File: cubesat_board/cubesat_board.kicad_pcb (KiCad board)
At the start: 2 copper layers, 90 x 90 mm, 2 parts, among them J1 CONN_02X26, J2 CONN_02X26

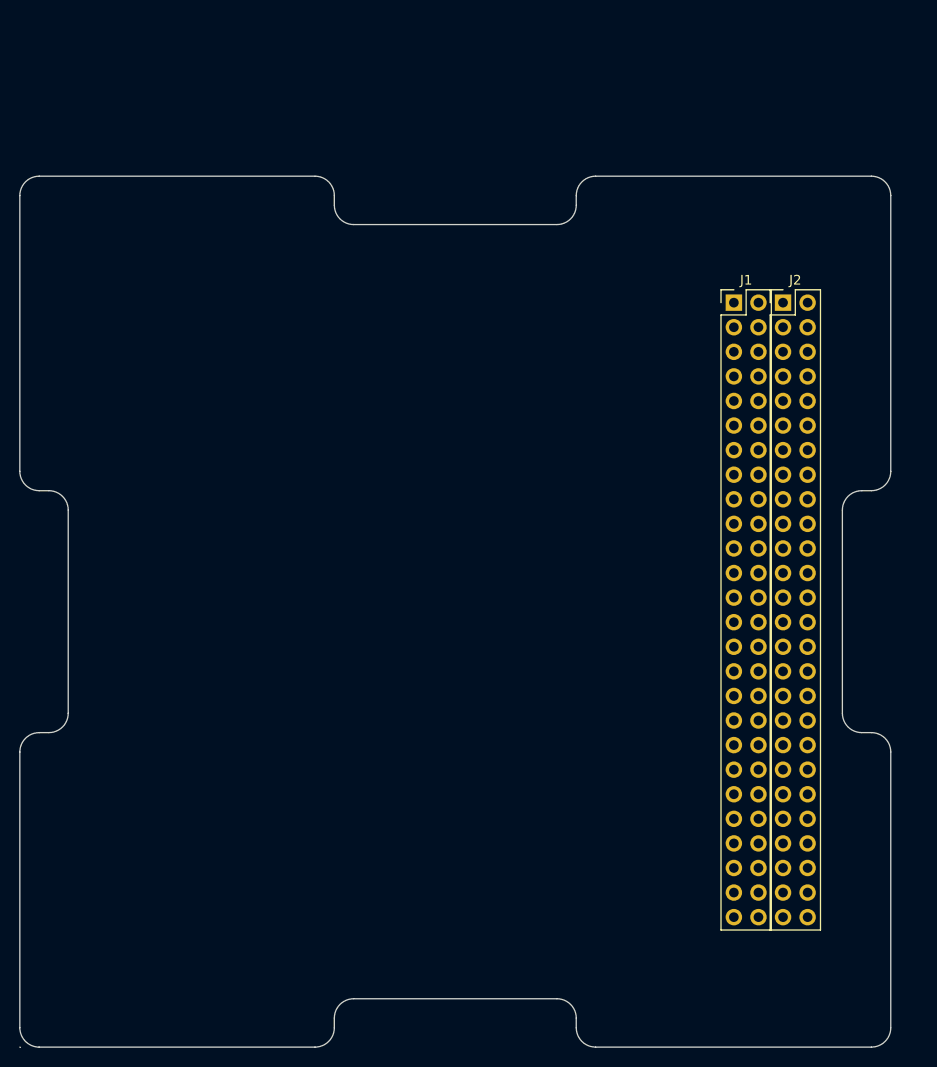
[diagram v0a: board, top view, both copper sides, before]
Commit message: New dxf without the slot behind the connector, updated board outline to new dxf and marked center of board as center of grids
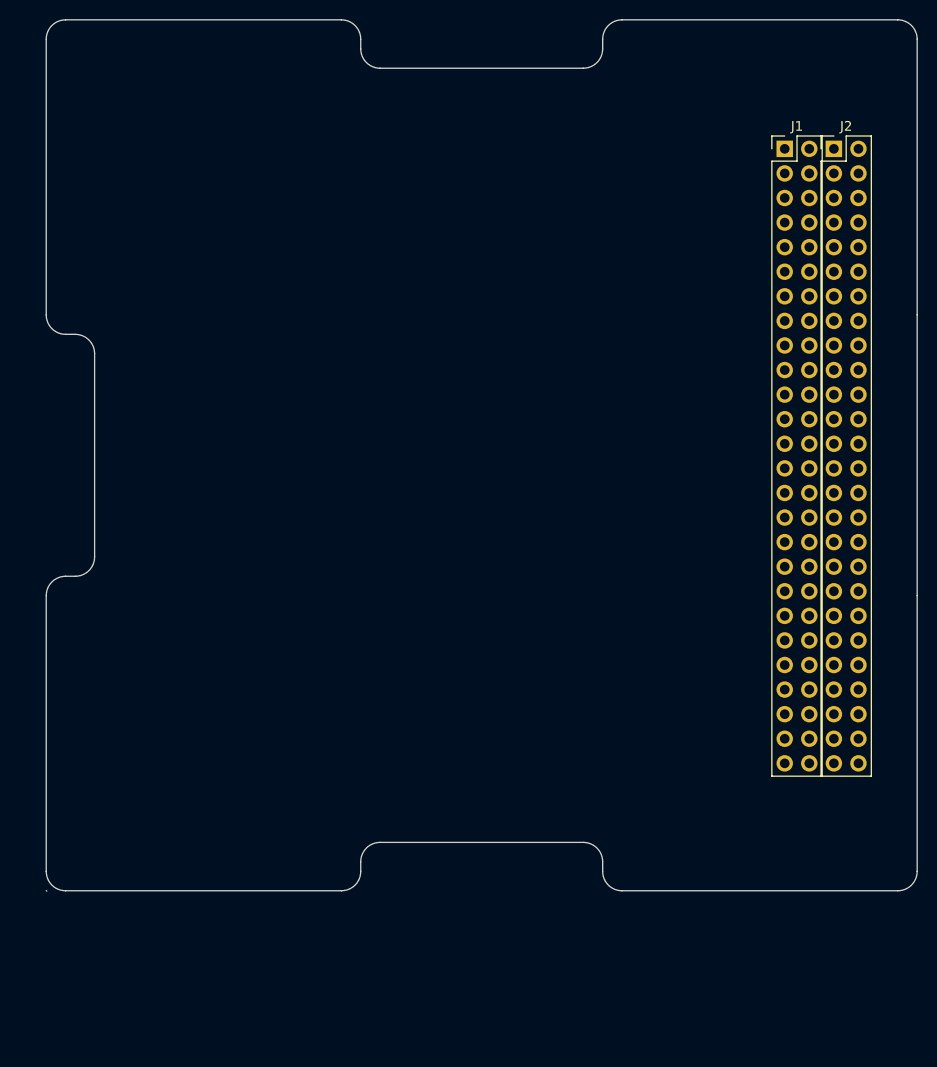
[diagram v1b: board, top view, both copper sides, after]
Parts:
- moved J2 16.7 mm to (172.9, 46.3)
- moved J1 16.7 mm to (167.8, 46.3)
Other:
- outline, holes or cut-outs redrawn
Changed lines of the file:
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@@
-(kicad_pcb (version 4) (host pcbnew 4.0.6)
+(kicad_pcb (version 4) (host pcbnew 4.0.7)
   (general
     (links 0)
     (no_connects 0)
-    (area 0 0 0 0)
+    (area 294.051667 73.53 309.198334 143.74)
     (thickness 1.6)
-    (drawings 41)
+    (drawings 35)
     (tracks 0)
     (zones 0)
@@
     (pad_drill 0.762)
     (pad_to_mask_clearance 0.2)
-    (aux_axis_origin 0 0)
-    (visible_elements FFFFFF7F)
+    (aux_axis_origin 136.5 78)
+    (grid_origin 136.5 78)
+    (visible_elements 7FFFFFFF)
     (pcbplotparams
       (layerselection 0x00030_80000001)
@@
   )
   (module Pin_Headers:Pin_Header_Straight_2x26_Pitch2.54mm (layer F.Cu)
-    (at 162.56 62.23)
+    (at 167.815 46.335)
     (descr "Through hole straight pin header, 2x26, 2.54mm pitch, double rows")
     (tags "Through hole pin header THT 2x26 2.54mm double row")
@@
   )
   (module Pin_Headers:Pin_Header_Straight_2x26_Pitch2.54mm (layer F.Cu)
-    (at 167.64 62.23)
+    (at 172.895 46.335)
     (descr "Through hole straight pin header, 2x26, 2.54mm pitch, double rows")
     (tags "Through hole pin header THT 2x26 2.54mm double row")
@@
     )
   )
-  (gr_line (start 91.773 106.660517) (end 90.773 106.660517) (layer Edge.Cuts) (width 0.1))
-  (gr_line (start 119.273 49.160517) (end 90.773 49.160517) (layer Edge.Cuts) (width 0.1))
-  (gr_line (start 178.773 79.660517) (end 178.773 51.160517) (layer Edge.Cuts) (width 0.1))
-  (gr_line (start 88.773 108.660517) (end 88.773 137.160517) (layer Edge.Cuts) (width 0.1))
-  (gr_line (start 88.773 51.160517) (end 88.773 79.660517) (layer Edge.Cuts) (width 0.1))
-  (gr_line (start 176.773 49.160517) (end 148.273 49.160517) (layer Edge.Cuts) (width 0.1))
-  (gr_line (start 146.273 52.160517) (end 146.273 51.160517) (layer Edge.Cuts) (width 0.1))
-  (gr_line (start 93.773 83.660517) (end 93.773 104.660517) (layer Edge.Cuts) (width 0.1))
-  (gr_line (start 121.273 52.160517) (end 121.273 51.160517) (layer Edge.Cuts) (width 0.1))
-  (gr_line (start 175.773 81.660517) (end 176.773 81.660517) (layer Edge.Cuts) (width 0.1))
-  (gr_line (start 88.773 139.160517) (end 88.832983 139.188433) (layer Edge.Cuts) (width 0.1))
-  (gr_line (start 90.773 81.660517) (end 91.773 81.660517) (layer Edge.Cuts) (width 0.1))
-  (gr_line (start 144.273 54.160517) (end 123.273 54.160517) (layer Edge.Cuts) (width 0.1))
-  (gr_arc (start 144.273 52.160517) (end 144.273 54.160517) (angle -90) (layer Edge.Cuts) (width 0.1))
-  (gr_line (start 148.273 139.160517) (end 176.773 139.160517) (layer Edge.Cuts) (width 0.1))
-  (gr_arc (start 175.773 104.660517) (end 173.773 104.660517) (angle -90) (layer Edge.Cuts) (width 0.1))
-  (gr_line (start 173.773 104.660517) (end 173.773 83.660517) (layer Edge.Cuts) (width 0.1))
-  (gr_arc (start 175.773 83.660517) (end 175.773 81.660517) (angle -90) (layer Edge.Cuts) (width 0.1))
-  (gr_arc (start 176.773 79.660517) (end 176.773 81.660517) (angle -90) (layer Edge.Cuts) (width 0.1))
-  (gr_line (start 146.273 136.160517) (end 146.273 137.160517) (layer Edge.Cuts) (width 0.1))
-  (gr_arc (start 90.773 108.660517) (end 90.773 106.660517) (angle -90) (layer Edge.Cuts) (width 0.1))
-  (gr_line (start 90.773 139.160517) (end 119.273 139.160517) (layer Edge.Cuts) (width 0.1))
-  (gr_line (start 176.773 106.660517) (end 175.773 106.660517) (layer Edge.Cuts) (width 0.1))
-  (gr_arc (start 176.773 51.160517) (end 178.773 51.160517) (angle -90) (layer Edge.Cuts) (width 0.1))
-  (gr_arc (start 148.273 137.160517) (end 146.273 137.160517) (angle -90) (layer Edge.Cuts) (width 0.1))
-  (gr_arc (start 90.773 79.660517) (end 88.773 79.660517) (angle -90) (layer Edge.Cuts) (width 0.1))
-  (gr_line (start 178.773 137.160517) (end 178.773 108.660517) (layer Edge.Cuts) (width 0.1))
-  (gr_arc (start 176.773 137.160517) (end 176.773 139.160517) (angle -90) (layer Edge.Cuts) (width 0.1))
-  (gr_arc (start 148.273 51.160517) (end 148.273 49.160517) (angle -90) (layer Edge.Cuts) (width 0.1))
-  (gr_arc (start 119.273 51.160517) (end 121.273 51.160517) (angle -90) (layer Edge.Cuts) (width 0.1))
-  (gr_arc (start 90.773 137.160517) (end 88.773 137.160517) (angle -90) (layer Edge.Cuts) (width 0.1))
-  (gr_line (start 123.273 134.160517) (end 144.273 134.160517) (layer Edge.Cuts) (width 0.1))
-  (gr_line (start 121.273 137.160517) (end 121.273 136.160517) (layer Edge.Cuts) (width 0.1))
-  (gr_arc (start 91.773 83.660517) (end 93.773 83.660517) (angle -90) (layer Edge.Cuts) (width 0.1))
-  (gr_arc (start 91.773 104.660517) (end 91.773 106.660517) (angle -90) (layer Edge.Cuts) (width 0.1))
-  (gr_arc (start 123.273 52.160517) (end 121.273 52.160517) (angle -90) (layer Edge.Cuts) (width 0.1))
-  (gr_arc (start 176.773 108.660517) (end 178.773 108.660517) (angle -90) (layer Edge.Cuts) (width 0.1))
-  (gr_arc (start 119.273 137.160517) (end 119.273 139.160517) (angle -90) (layer Edge.Cuts) (width 0.1))
-  (gr_arc (start 123.273 136.160517) (end 123.273 134.160517) (angle -90) (layer Edge.Cuts) (width 0.1))
-  (gr_arc (start 144.273 136.160517) (end 146.273 136.160517) (angle -90) (layer Edge.Cuts) (width 0.1))
-  (gr_arc (start 90.773 51.160517) (end 90.773 49.160517) (angle -90) (layer Edge.Cuts) (width 0.1))
+  (gr_line (start 91.5011 123.0036) (end 91.561083 123.031516) (layer Edge.Cuts) (width 0.1))
+  (gr_line (start 151.0011 123.0036) (end 179.5011 123.0036) (layer Edge.Cuts) (width 0.1))
+  (gr_line (start 93.5011 123.0036) (end 122.0011 123.0036) (layer Edge.Cuts) (width 0.1))
+  (gr_arc (start 122.0011 121.0036) (end 122.0011 123.0036) (angle -90) (layer Edge.Cuts) (width 0.1))
+  (gr_arc (start 179.5011 121.0036) (end 179.5011 123.0036) (angle -90) (layer Edge.Cuts) (width 0.1))
+  (gr_line (start 149.0011 36.0036) (end 149.0011 35.0036) (layer Edge.Cuts) (width 0.1))
+  (gr_line (start 91.5011 92.5036) (end 91.5011 121.0036) (layer Edge.Cuts) (width 0.1))
+  (gr_line (start 94.5011 90.5036) (end 93.5011 90.5036) (layer Edge.Cuts) (width 0.1))
+  (gr_line (start 96.5011 67.5036) (end 96.5011 88.5036) (layer Edge.Cuts) (width 0.1))
+  (gr_line (start 93.5011 65.5036) (end 94.5011 65.5036) (layer Edge.Cuts) (width 0.1))
+  (gr_line (start 91.5011 35.0036) (end 91.5011 63.5036) (layer Edge.Cuts) (width 0.1))
+  (gr_line (start 122.0011 33.0036) (end 93.5011 33.0036) (layer Edge.Cuts) (width 0.1))
+  (gr_line (start 124.0011 36.0036) (end 124.0011 35.0036) (layer Edge.Cuts) (width 0.1))
+  (gr_line (start 147.0011 38.0036) (end 126.0011 38.0036) (layer Edge.Cuts) (width 0.1))
+  (gr_line (start 179.5011 33.0036) (end 151.0011 33.0036) (layer Edge.Cuts) (width 0.1))
+  (gr_line (start 181.5011 63.5036) (end 181.5011 35.0036) (layer Edge.Cuts) (width 0.1))
+  (gr_line (start 181.5011 63.5036) (end 181.5011 92.5036) (layer Edge.Cuts) (width 0.1))
+  (gr_line (start 181.5011 121.0036) (end 181.5011 92.5036) (layer Edge.Cuts) (width 0.1))
+  (gr_line (start 149.0011 120.0036) (end 149.0011 121.0036) (layer Edge.Cuts) (width 0.1))
+  (gr_line (start 126.0011 118.0036) (end 147.0011 118.0036) (layer Edge.Cuts) (width 0.1))
+  (gr_line (start 124.0011 121.0036) (end 124.0011 120.0036) (layer Edge.Cuts) (width 0.1))
+  (gr_arc (start 93.5011 63.5036) (end 91.5011 63.5036) (angle -90) (layer Edge.Cuts) (width 0.1))
+  (gr_arc (start 94.5011 67.5036) (end 96.5011 67.5036) (angle -90) (layer Edge.Cuts) (width 0.1))
+  (gr_arc (start 94.5011 88.5036) (end 94.5011 90.5036) (angle -90) (layer Edge.Cuts) (width 0.1))
+  (gr_arc (start 93.5011 92.5036) (end 93.5011 90.5036) (angle -90) (layer Edge.Cuts) (width 0.1))
+  (gr_arc (start 126.0011 120.0036) (end 126.0011 118.0036) (angle -90) (layer Edge.Cuts) (width 0.1))
+  (gr_arc (start 147.0011 120.0036) (end 149.0011 120.0036) (angle -90) (layer Edge.Cuts) (width 0.1))
+  (gr_arc (start 151.0011 121.0036) (end 149.0011 121.0036) (angle -90) (layer Edge.Cuts) (width 0.1))
+  (gr_arc (start 151.0011 35.0036) (end 151.0011 33.0036) (angle -90) (layer Edge.Cuts) (width 0.1))
+  (gr_arc (start 147.0011 36.0036) (end 147.0011 38.0036) (angle -90) (layer Edge.Cuts) (width 0.1))
+  (gr_arc (start 126.0011 36.0036) (end 124.0011 36.0036) (angle -90) (layer Edge.Cuts) (width 0.1))
+  (gr_arc (start 122.0011 35.0036) (end 124.0011 35.0036) (angle -90) (layer Edge.Cuts) (width 0.1))
+  (gr_arc (start 93.5011 35.0036) (end 93.5011 33.0036) (angle -90) (layer Edge.Cuts) (width 0.1))
+  (gr_arc (start 179.5011 35.0036) (end 181.5011 35.0036) (angle -90) (layer Edge.Cuts) (width 0.1))
+  (gr_arc (start 93.5011 121.0036) (end 91.5011 121.0036) (angle -90) (layer Edge.Cuts) (width 0.1))
 )

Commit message: Created new cubesat board outline, and created draft and step model to be used for vibes analysis
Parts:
- moved J1 91.6 mm to (254.3, 16.3)
- moved J2 91.6 mm to (259.4, 16.3)
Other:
- board size 90 x 90 mm -> 91.4 x 91.4 mm
